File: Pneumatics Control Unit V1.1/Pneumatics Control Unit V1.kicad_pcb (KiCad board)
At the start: 2 copper layers, 53.6 x 69.2 mm, 76 parts, among them J1 TX_PORT, J10 Conn_01x02_Male, J11 Conn_01x02_Male, J12 10118194-0001LF, J2 RX_PORT, J3 MICROMOD-2222, J4 Conn_01x02_Male, J5 Conn_01x02_Male, J6 Conn_01x02_Male, J7 Conn_01x02_Male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

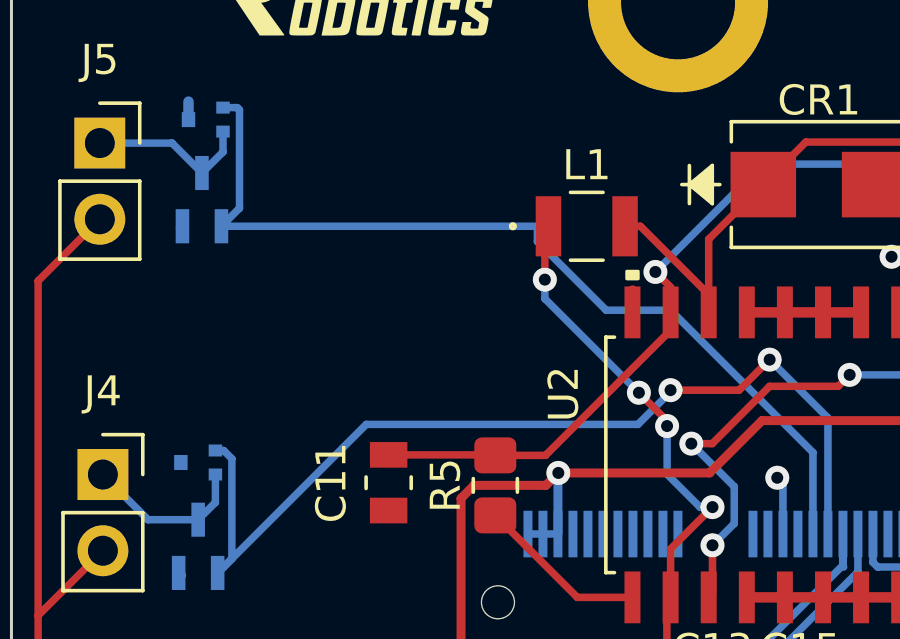
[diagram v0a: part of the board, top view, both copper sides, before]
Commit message: Adding some caps to the switching and clearing errors
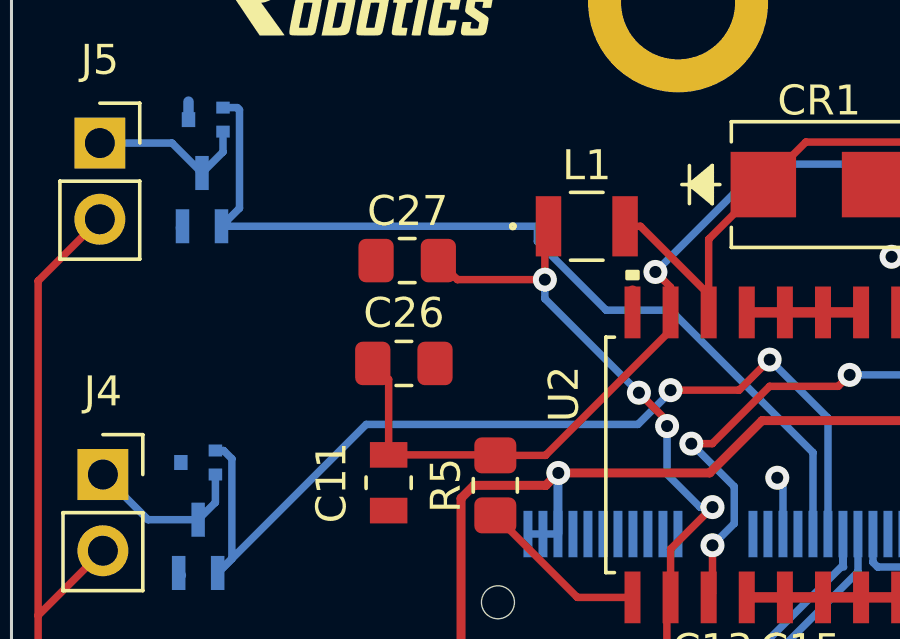
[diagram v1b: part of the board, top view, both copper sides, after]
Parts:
- added C26: 1u, Capacitor_SMD:C_0805_2012Metric_Pad1.18x1.45mm_HandSolder, F.Cu at (116.8, 83.8)
- added C27: 0.1u, Capacitor_SMD:C_0805_2012Metric_Pad1.18x1.45mm_HandSolder, F.Cu at (117.0, 80.4)
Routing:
- net /220uF: track 47.6 -> 51.4 mm
- net /RS485_A_12V: track 84.7 -> 87.9 mm

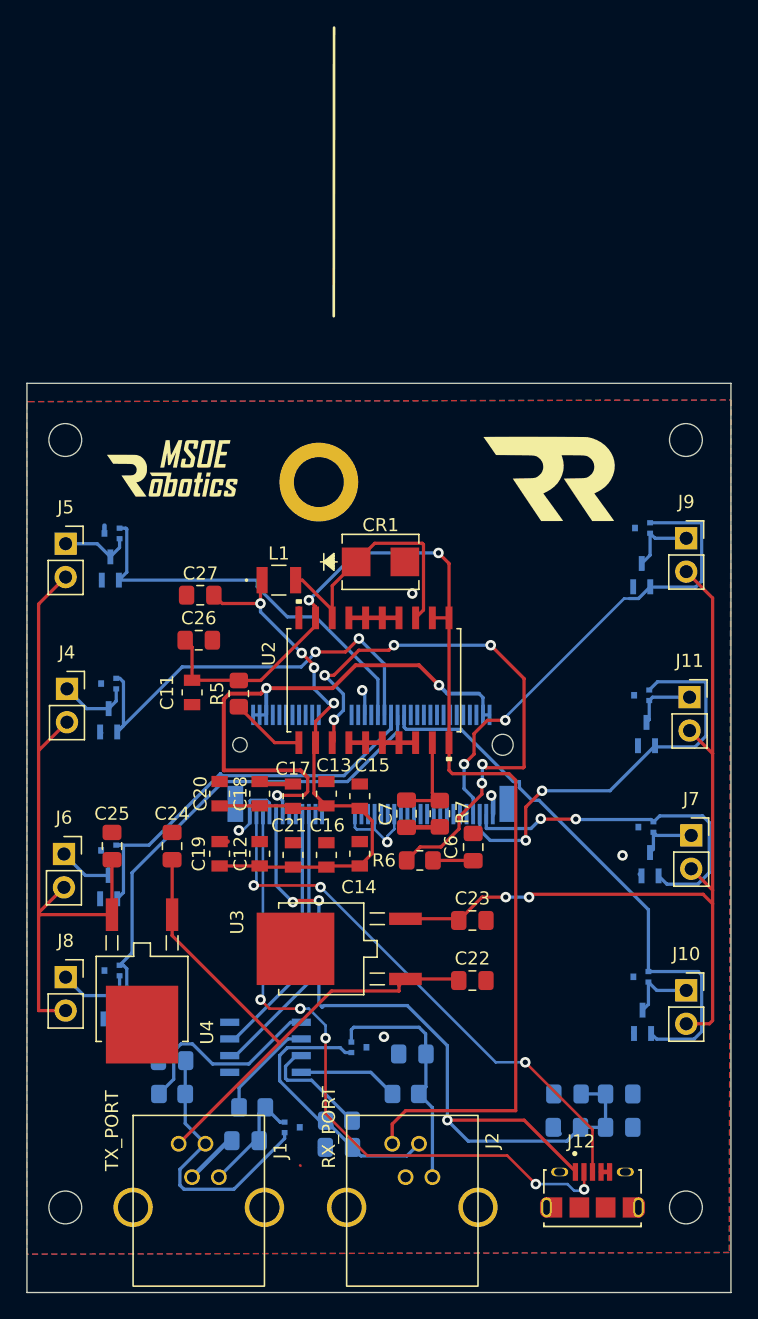
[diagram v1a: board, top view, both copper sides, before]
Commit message: Slimming the rectangle
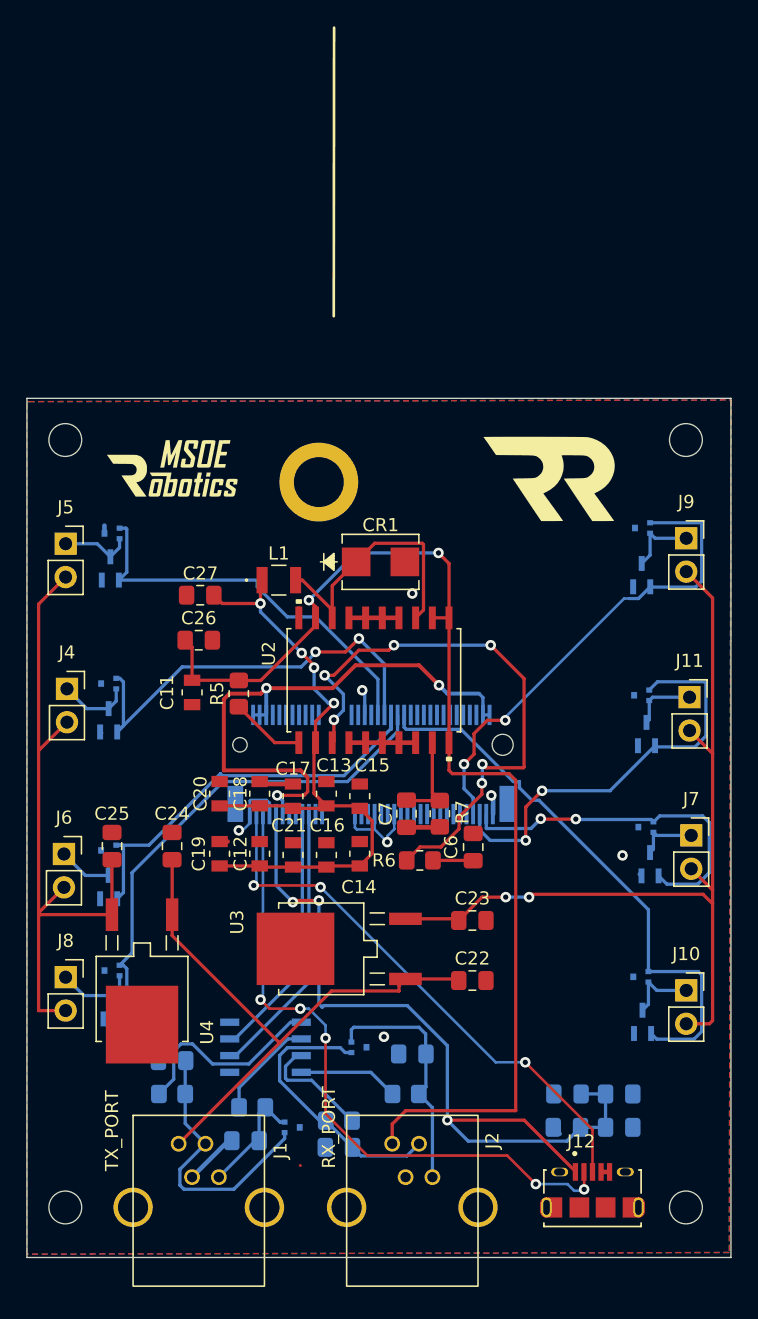
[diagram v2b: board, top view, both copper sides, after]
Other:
- board size 53.6 x 69.2 mm -> 53.6 x 65.4 mm
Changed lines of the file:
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@@
     (fp_arc (start 11 19) (mid 10.7 19.7) (end 10 20) (layer "B.Fab") (width 0.05))
     (fp_arc (start 3.225 1.9) (mid 2.625 2.5) (end 2.025 1.9) (layer "B.Fab") (width 0.0508))
-    (fp_arc (start 10.4 3) (mid 10.065368 2.842287) (end 9.925 2.5) (layer "B.Fab") (width 0.0508))
+    (fp_arc (start 10.4 3) (mid 10.065362 2.842281) (end 9.925 2.5) (layer "B.Fab") (width 0.0508))
     (fp_arc (start -9.925 2.5) (mid -10.066759 2.840954) (end -10.4 3) (layer "B.Fab") (width 0.0508))
     (fp_arc (start -10 20) (mid -10.7 19.7) (end -11 19) (layer "B.Fab") (width 0.05))
@@
   )
   (gr_line (start 127.1414 37.1856) (end 127.116 59.1566) (layer "F.SilkS") (width 0.2032))
-  (gr_rect (start 103.759 64.262) (end 157.353 133.477) (layer "Edge.Cuts") (width 0.1) (fill none))
+  (gr_rect (start 103.759 65.405) (end 157.353 130.81) (layer "Edge.Cuts") (width 0.1) (fill none))
   (gr_rect (start 103.632 65.532) (end 157.48 130.556) (layer "User.6") (width 0.15) (fill none))
   (gr_text "Andrew Kempen\nAsher Sprigler\nNathan Roth\n4/5/2022" (at 114.808 70.612) (layer "B.SilkS")

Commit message: Removing random line
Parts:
- moved G*** 2.50 mm to (141.2, 72.1)
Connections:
- net 5V renamed 5V_R

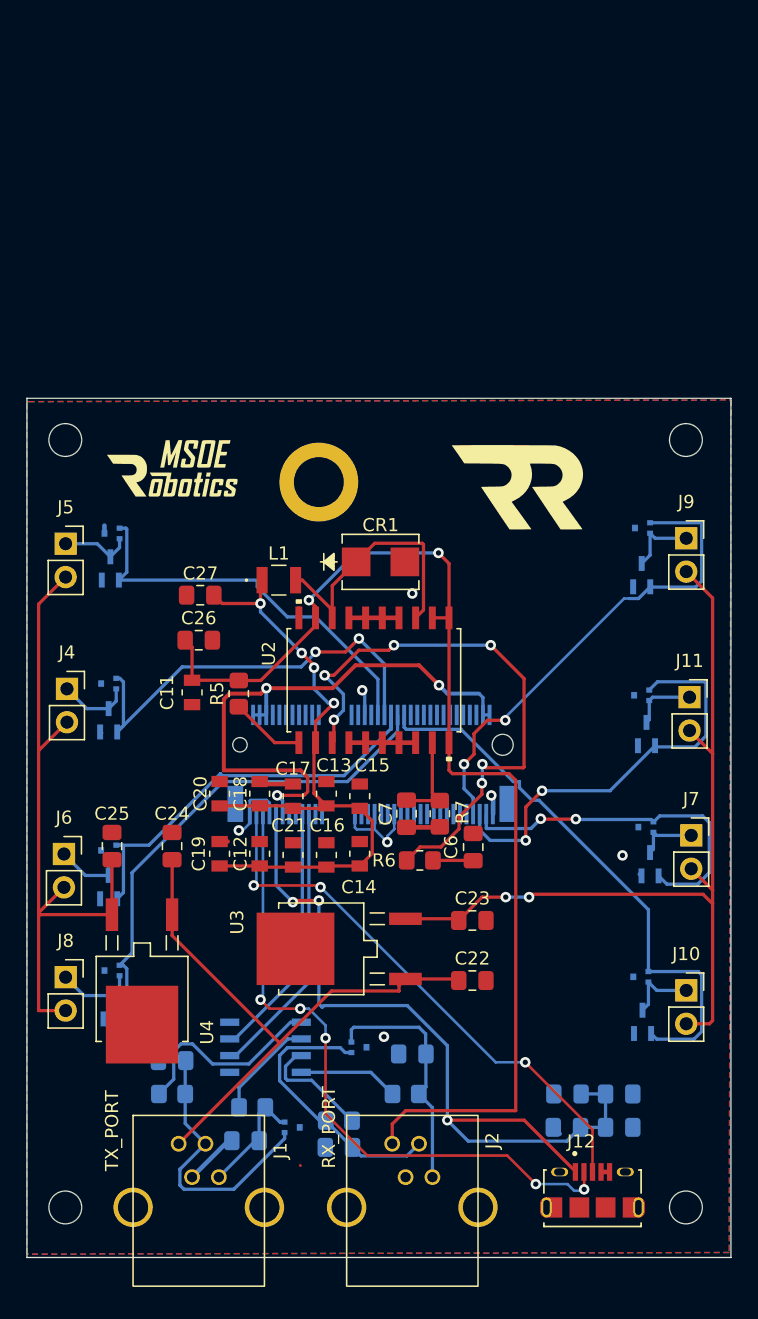
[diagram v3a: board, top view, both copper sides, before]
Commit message: Reducing vias, Thicken traces, adding resistors
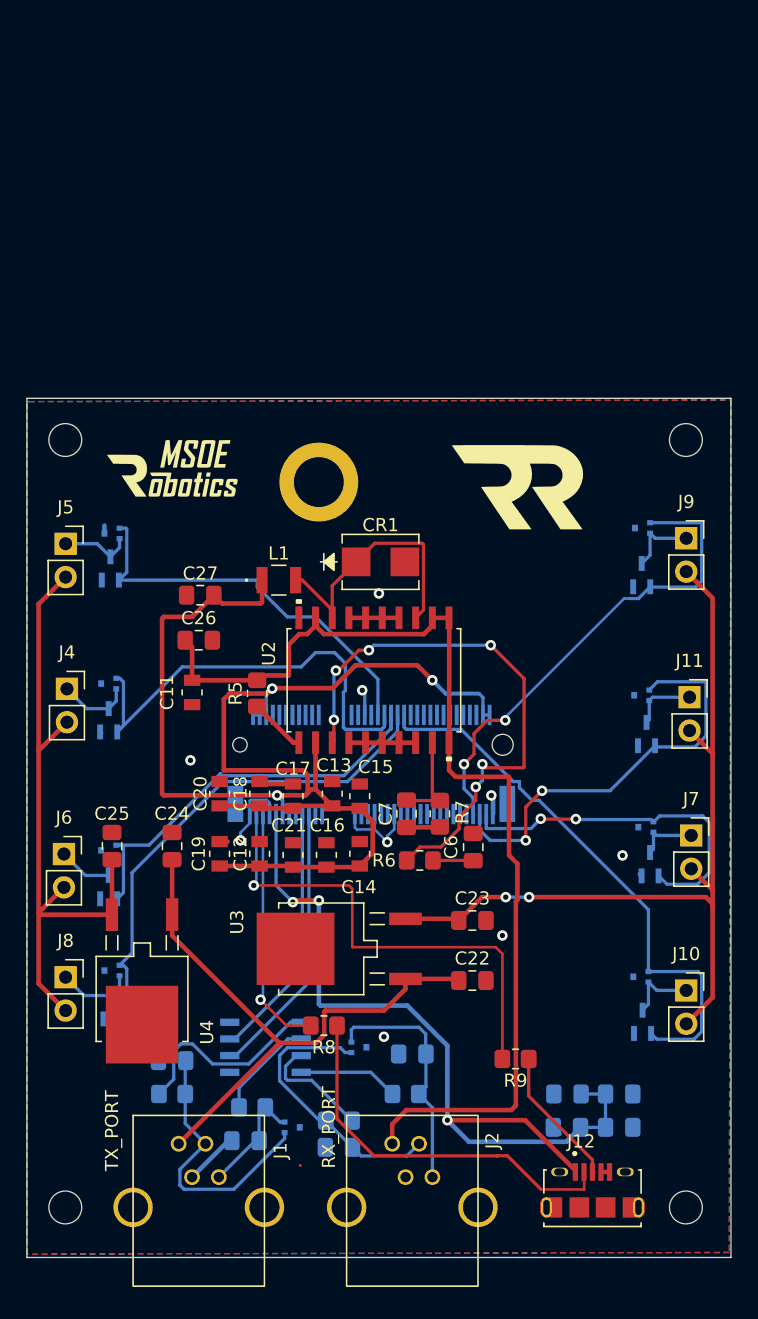
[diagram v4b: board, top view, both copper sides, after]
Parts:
- added R8: 27, Resistor_SMD:R_0805_2012Metric_Pad1.20x1.40mm_HandSolder, F.Cu at (126.4, 113.2)
- added R9: 27, Resistor_SMD:R_0805_2012Metric_Pad1.20x1.40mm_HandSolder, F.Cu at (141.0, 115.7)
- moved R5 1.40 mm to (121.3, 87.9)
- moved C13 0.44 mm to (127.0, 95.5)
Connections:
- C12 pad 1: /220uF -> 3.3V
- C13 pad 1: /220uF -> 3.3V
- C14 pad 1: /220uF -> 3.3V
- C15 pad 1: /220uF -> 3.3V
- C16 pad 1: /220uF -> 3.3V
- C17 pad 1: /220uF -> 3.3V
- C18 pad 1: /220uF -> 3.3V
- C19 pad 1: /220uF -> 3.3V
- C20 pad 1: /220uF -> 3.3V
- C21 pad 1: /220uF -> 3.3V
- C27 pad 1: /220uF -> 3.3V
- J12 pad 2: /USB_D- -> Net-(J12-Pad2)
- J12 pad 3: /USB_D+ -> Net-(J12-Pad3)
- J3 pad 11: Net-(J3-Pad11) -> 3.3V
- J3 pad 2: Net-(J3-Pad11) -> 3.3V
- J3 pad 4: Net-(J3-Pad11) -> 3.3V
- J3 pad 6: Net-(J3-Pad11) -> 3.3V
- J3 pad 72: Net-(J3-Pad11) -> 3.3V
- J3 pad 74: Net-(J3-Pad11) -> 3.3V
- L1 pad 1: /220uF -> 3.3V
- U2 pad 12: /220uF -> 3.3V
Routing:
- net 3.3V: track 0.00 -> 123.4 mm, vias 0 -> 3
- net /220uF: track 51.4 -> 0.00 mm, vias 4 -> 0
- net Net-(J3-Pad11): track 44.1 -> 0.00 mm, vias 3 -> 0
- net /USB_D-: track 50.2 -> 18.8 mm, vias 5 -> 1
- net Net-(J12-Pad2): track 0.00 -> 29.5 mm
- net Net-(J12-Pad3): track 0.00 -> 10.6 mm
- net /RS485_A_12V: track 87.9 -> 80.9 mm, vias 2 -> 0
- net /USB_D+: track 42.2 -> 37.2 mm, vias 3 -> 1
- net Net-(R6-Pad1): track 43.9 -> 42.5 mm
- net Net-(R5-Pad1): track 5.70 -> 4.31 mm
- net /GPIO_1: track 32.7 -> 34.0 mm, vias 2 -> 0
- net /RS485_B_12V: track 44.2 -> 45.4 mm
- net 5V_L: track 51.5 -> 50.3 mm
- net GND: track 43.3 -> 43.8 mm, vias 7 -> 9

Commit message: Moved via, cleaning traces
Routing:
- net GND: track 43.8 -> 37.9 mm
- net 3.3V: track 123.4 -> 122.8 mm
